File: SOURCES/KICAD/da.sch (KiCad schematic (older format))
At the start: 176 parts, among them IC301 IC_OPA1652AIDR, IC302 IC_OPA1652AIDR, IC303 IC_OPA1652AIDR, IC304 IC_OPA1652AIDR, IC305 IC_AK4458VN, IC306 IC_OPA1652AIDR, IC307 IC_OPA1652AIDR, IC308 IC_OPA1652AIDR, IC309 IC_OPA1652AIDR, X301 CONN_02X13

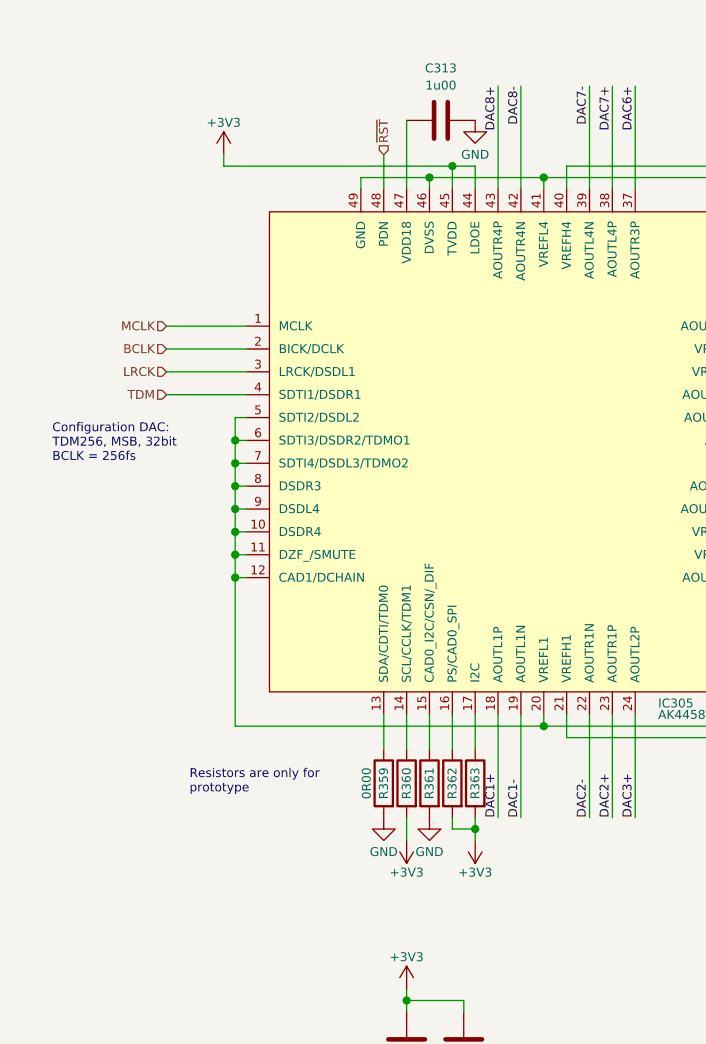
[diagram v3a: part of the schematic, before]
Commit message: I2C control of DAC
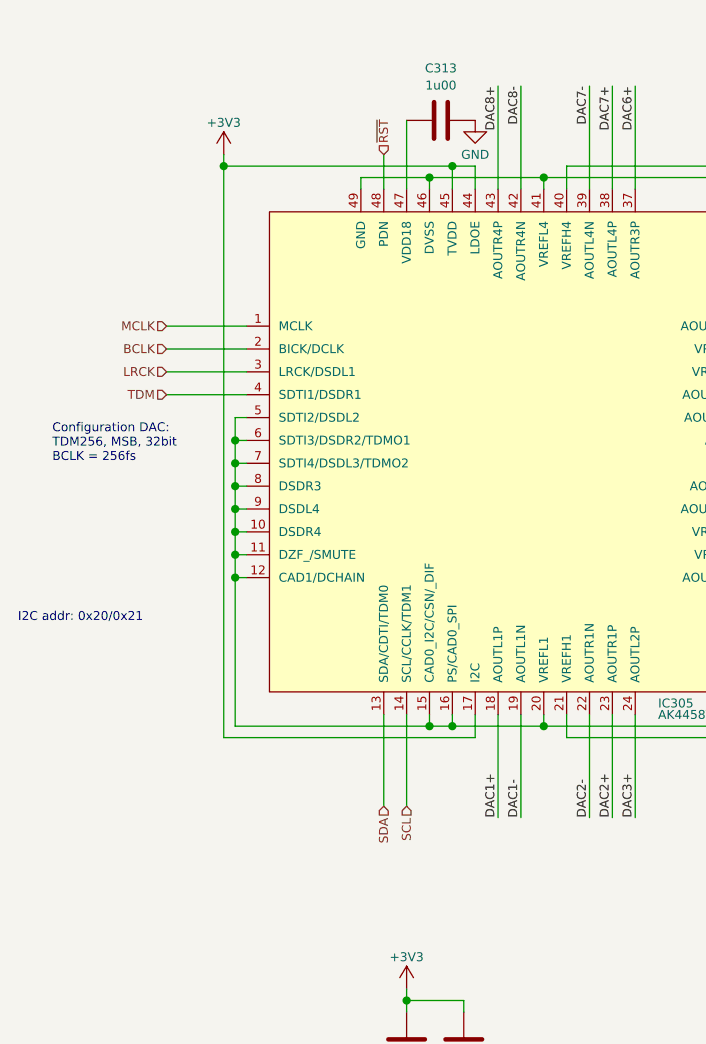
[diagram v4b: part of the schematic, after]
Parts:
- removed R359, R360, R361, R362, R363: RES_0R00_1%_0.125W_Thick_0805, rklib:C0805-RES, symbol rk:RES_0R00_1%_0.125W_Thick_0805
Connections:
- net +3V3: now also IC305.17 (I2C)
- net GND: now also IC305.15 (CAD0_I2C/CSN/_DIF), IC305.16 (PS/CAD0_SPI)
- net SDA: now reaches IC305.13 (SDA/CDTI/TDM0)
- net SCL: now reaches IC305.14 (SCL/CCLK/TDM1)
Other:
- note added: "I2C addr: 0x20/0x21"
- note removed: "Resistors are only for\nprototype"
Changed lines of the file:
@@
 Text Notes 1950 5000 0    39   ~ 0
 Configuration DAC:\nTDM256, MSB, 32bit\nBCLK = 256fs
-$Comp
-L freeDSP-aurora-rescue:GND #PWR0157
-U 1 1 590870EC
-P 3400 6550
-F 0 "#PWR0157" H 3400 6300 50  0001 C CNN
-F 1 "GND" H 3400 6400 39  0000 C CNN
-F 2 "" H 3400 6550 50  0000 C CNN
-F 3 "" H 3400 6550 50  0000 C CNN
-	1    3400 6550
-	1    0    0    -1
-$EndComp
-$Comp
-L freeDSP-aurora-rescue:+3V3 #PWR0158
-U 1 1 5908711B
-P 3500 6650
-F 0 "#PWR0158" H 3500 6500 50  0001 C CNN
-F 1 "+3V3" H 3500 6790 39  0000 C CNN
-F 2 "" H 3500 6650 50  0000 C CNN
-F 3 "" H 3500 6650 50  0000 C CNN
-	1    3500 6650
-	-1   0    0    1
-$EndComp
 Wire Wire Line
-	3400 6250 3400 6100
+	3400 6500 3400 6100
 Wire Wire Line
-	3500 6250 3500 6100
-Wire Wire Line
-	3500 6650 3500 6550
-$Comp
-L freeDSP-aurora-rescue:GND #PWR0159
-U 1 1 5908737E
-P 3600 6550
-F 0 "#PWR0159" H 3600 6300 50  0001 C CNN
-F 1 "GND" H 3600 6400 39  0000 C CNN
-F 2 "" H 3600 6550 50  0000 C CNN
-F 3 "" H 3600 6550 50  0000 C CNN
-	1    3600 6550
-	1    0    0    -1
-$EndComp
+	3500 6500 3500 6100
 Wire Wire Line
-	3600 6100 3600 6250
+	3600 6100 3600 6150
 Wire Wire Line
 	2750 5500 2800 5500
 Wire Wire Line
 	2750 4800 2750 4900
-Wire Wire Line
-	2750 6150 4100 6150
 Connection ~ 5150 6150
-$Comp
-L freeDSP-aurora-rescue:+3V3 #PWR0160
-U 1 1 590874C4
-P 3800 6650
-F 0 "#PWR0160" H 3800 6500 50  0001 C CNN
-F 1 "+3V3" H 3800 6790 39  0000 C CNN
-F 2 "" H 3800 6650 50  0000 C CNN
-F 3 "" H 3800 6650 50  0000 C CNN
-	1    3800 6650
-	-1   0    0    1
-$EndComp
-Wire Wire Line
-	3800 6550 3800 6600
-Wire Wire Line
-	3800 6600 3700 6600
 Wire Wire Line
-	3700 6600 3700 6550
-Connection ~ 3800 6600
-Wire Wire Line
-	3700 6250 3700 6100
-Wire Wire Line
-	3800 6250 3800 6100
-Text Notes 2550 6450 0    39   ~ 0
-Resistors are only for\nprototype
+	3800 6200 3800 6100
+Text Notes 1800 5700 0    39   ~ 0
+I2C addr: 0x20/0x21
 Wire Wire Line
 	2750 5400 2800 5400
@@
 	5150 6150 5150 6250
 Wire Wire Line
-	3800 6600 3800 6650
-Wire Wire Line
 	2750 5500 2750 6150
 Wire Wire Line
@@
 $EndComp
 $Comp
-L rk:RES_0R00_1%_0.125W_Thick_0805 R?
-U 1 1 60D522C8
-P 3400 6400
-AR Path="/5904EED2/60D522C8" Ref="R?"  Part="1"
-AR Path="/5904EED5/60D522C8" Ref="R359"  Part="1"
-F 0 "R359" H 3400 6400 39  0000 C CNN
-F 1 "RES_0R00_1%_0.125W_Thick_0805" H 3400 6225 39  0001 C CNN
-F 2 "rklib:C0805-RES" H 3400 6175 39  0001 C CNN
-F 3 "" H 3400 6400 50  0000 C CNN
-F 4 "0R00" H 3400 6475 39  0000 C CNN "Value1"
-F 5 "1% 0.125W Thick" H 3400 6275 39  0001 C CNN "Value2"
-F 6 "311-0.0ARCT-ND" H 3400 6100 39  0001 C CNN "digikey"
-F 7 "Yageo" H 0   0   50  0001 C CNN "Manufacturer"
-F 8 "RC0805JR-070RL" H 0   0   50  0001 C CNN "pn"
-	1    3400 6400
-	0    -1   1    0
-$EndComp
-$Comp
-L rk:RES_0R00_1%_0.125W_Thick_0805 R?
-U 1 1 60D9ABC3
-P 3500 6400
-AR Path="/5904EED2/60D9ABC3" Ref="R?"  Part="1"
-AR Path="/5904EED5/60D9ABC3" Ref="R360"  Part="1"
-F 0 "R360" H 3500 6400 39  0000 C CNN
-F 1 "RES_0R00_1%_0.125W_Thick_0805" H 3500 6225 39  0001 C CNN
-F 2 "rklib:C0805-RES" H 3500 6175 39  0001 C CNN
-F 3 "" H 3500 6400 50  0000 C CNN
-F 4 "0R00" H 3500 6475 39  0001 C CNN "Value1"
-F 5 "1% 0.125W Thick" H 3500 6275 39  0001 C CNN "Value2"
-F 6 "311-0.0ARCT-ND" H 3500 6100 39  0001 C CNN "digikey"
-F 7 "Yageo" H 0   0   50  0001 C CNN "Manufacturer"
-F 8 "RC0805JR-070RL" H 0   0   50  0001 C CNN "pn"
-	1    3500 6400
-	0    -1   1    0
-$EndComp
-$Comp
-L rk:RES_0R00_1%_0.125W_Thick_0805 R?
-U 1 1 60DE2F2F
-P 3600 6400
-AR Path="/5904EED2/60DE2F2F" Ref="R?"  Part="1"
-AR Path="/5904EED5/60DE2F2F" Ref="R361"  Part="1"
-F 0 "R361" H 3600 6400 39  0000 C CNN
-F 1 "RES_0R00_1%_0.125W_Thick_0805" H 3600 6225 39  0001 C CNN
-F 2 "rklib:C0805-RES" H 3600 6175 39  0001 C CNN
-F 3 "" H 3600 6400 50  0000 C CNN
-F 4 "0R00" H 3600 6475 39  0001 C CNN "Value1"
-F 5 "1% 0.125W Thick" H 3600 6275 39  0001 C CNN "Value2"
-F 6 "311-0.0ARCT-ND" H 3600 6100 39  0001 C CNN "digikey"
-F 7 "Yageo" H 0   0   50  0001 C CNN "Manufacturer"
-F 8 "RC0805JR-070RL" H 0   0   50  0001 C CNN "pn"
-	1    3600 6400
-	0    -1   1    0
-$EndComp
-$Comp
-L rk:RES_0R00_1%_0.125W_Thick_0805 R?
-U 1 1 60E2ADED
-P 3700 6400
-AR Path="/5904EED2/60E2ADED" Ref="R?"  Part="1"
-AR Path="/5904EED5/60E2ADED" Ref="R362"  Part="1"
-F 0 "R362" H 3700 6400 39  0000 C CNN
-F 1 "RES_0R00_1%_0.125W_Thick_0805" H 3700 6225 39  0001 C CNN
-F 2 "rklib:C0805-RES" H 3700 6175 39  0001 C CNN
-F 3 "" H 3700 6400 50  0000 C CNN
-F 4 "0R00" H 3700 6475 39  0001 C CNN "Value1"
-F 5 "1% 0.125W Thick" H 3700 6275 39  0001 C CNN "Value2"
-F 6 "311-0.0ARCT-ND" H 3700 6100 39  0001 C CNN "digikey"
-F 7 "Yageo" H 0   0   50  0001 C CNN "Manufacturer"
-F 8 "RC0805JR-070RL" H 0   0   50  0001 C CNN "pn"
-	1    3700 6400
-	0    -1   1    0
-$EndComp
-$Comp
-L rk:RES_0R00_1%_0.125W_Thick_0805 R?
-U 1 1 60E72CAB
-P 3800 6400
-AR Path="/5904EED2/60E72CAB" Ref="R?"  Part="1"
-AR Path="/5904EED5/60E72CAB" Ref="R363"  Part="1"
-F 0 "R363" H 3800 6400 39  0000 C CNN
-F 1 "RES_0R00_1%_0.125W_Thick_0805" H 3800 6225 39  0001 C CNN
-F 2 "rklib:C0805-RES" H 3800 6175 39  0001 C CNN
-F 3 "" H 3800 6400 50  0000 C CNN
-F 4 "0R00" H 3800 6475 39  0001 C CNN "Value1"
-F 5 "1% 0.125W Thick" H 3800 6275 39  0001 C CNN "Value2"
-F 6 "311-0.0ARCT-ND" H 3800 6100 39  0001 C CNN "digikey"
-F 7 "Yageo" H 0   0   50  0001 C CNN "Manufacturer"
-F 8 "RC0805JR-070RL" H 0   0   50  0001 C CNN "pn"
-	1    3800 6400
-	0    -1   1    0
-$EndComp
-$Comp
 L rk:IC_OPA1652AIDR IC?
 U 1 1 5C38DC62
@@
 	1    0    0    -1
 $EndComp
+Text HLabel 3400 6500 3    39   Input ~ 0
+SDA
+Text HLabel 3500 6500 3    39   Input ~ 0
+SCL
+Wire Wire Line
+	3800 6200 2700 6200
+Wire Wire Line
+	2700 6200 2700 3700
+Connection ~ 2700 3700
+Wire Wire Line
+	2750 6150 3600 6150
+Connection ~ 3600 6150
+Wire Wire Line
+	3600 6150 3700 6150
+Wire Wire Line
+	3700 6100 3700 6150
+Connection ~ 3700 6150
+Wire Wire Line
+	3700 6150 4100 6150
 $EndSCHEMATC

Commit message: Optimized ground plane
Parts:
- X301: footprint rklib:HDR_02x13 -> rklib:IDC26; symbol freeDSP-aurora-rescue:CONN_02X13 -> rk:CON_IDC26
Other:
- note removed: "Achtung: Kanäle L/R vertauscht. Im SigmaDSP-Programm berücksichtigen!"
- moved on the sheet: C301, C302, C303, C304, C305, C306, C307, C308, C309, C310, C311, C312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

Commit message: Updated BOM
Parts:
- X301: value CONN_02X13 -> CON_IDC26; Manufacturer Sullins Connector Solutions -> Bud Industries; Value1 SKT_02x13 -> IDC26; digikey ??? -> 377-2269-ND; pn PRPC013DAAN-RC -> BC-32677
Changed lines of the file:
@@
 AOUT8+
 $Comp
-L rk:CON_IDC26 X301
-U 1 1 590CA412
-P 15000 4450
-F 0 "X301" H 15000 5150 39  0000 C CNN
-F 1 "CONN_02X13" V 15000 4450 39  0000 C CNN
-F 2 "rklib:IDC26" H 15000 3300 50  0001 C CNN
-F 3 "" H 15000 3300 50  0000 C CNN
-F 4 "SKT_02x13" H 1400 -4200 50  0001 C CNN "Value1"
-F 5 "-" H 1400 -4200 50  0001 C CNN "Value2"
-F 6 "???" H 1400 -4200 50  0001 C CNN "digikey"
-F 7 "Sullins Connector Solutions" H 1400 -4200 50  0001 C CNN "Manufacturer"
-F 8 "PRPC013DAAN-RC" H 1400 -4200 50  0001 C CNN "pn"
-	1    15000 4450
-	1    0    0    -1
-$EndComp
-$Comp
 L freeDSP-aurora-rescue:GND #PWR0189
 U 1 1 590CAA26
@@
 Wire Wire Line
 	2350 6200 2750 6200
+$Comp
+L rk:CON_IDC26 X301
+U 1 1 5CB47C29
+P 15000 4450
+F 0 "X301" H 15000 5243 39  0000 C CNN
+F 1 "CON_IDC26" H 15000 3700 39  0001 C CNN
+F 2 "rklib:IDC26" H 15050 3650 39  0001 C CNN
+F 3 "~" H 14950 4450 50  0001 C CNN
+F 4 "IDC26" H 15000 5168 39  0000 C CNN "Value1"
+F 5 "377-2269-ND" H 15000 3600 39  0001 C CNN "digikey"
+F 6 "Bud Industries" H 0   0   50  0001 C CNN "Manufacturer"
+F 7 "-" H 0   0   50  0001 C CNN "Value2"
+F 8 "BC-32677" H 0   0   50  0001 C CNN "pn"
+	1    15000 4450
+	1    0    0    -1
+$EndComp
 $EndSCHEMATC
